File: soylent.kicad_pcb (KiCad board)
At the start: 2 copper layers, 33 x 42.2 mm, 31 parts, among them J1 DB9_Female, J2 Conn_01x04, J3 Conn_01x04, J4 Conn_02x03_Counter_Clockwise, Q1 BC847, Q2 BC847, U1 ATtiny202-SS, U2 MIC5504-3.3YM5, U3 LM2776, U4 MAX3188EEUT+T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

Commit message: Shrink required board area
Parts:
- moved J4 5.50 mm to (236.7, 30.7)
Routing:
- net Net-(J4-Pad1): track 9.78 -> 5.02 mm
- net Net-(J4-Pad3): track 13.6 -> 9.86 mm
- net Net-(J4-Pad2): track 12.9 -> 9.75 mm
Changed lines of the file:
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@@
     (thickness 1.6)
     (drawings 6)
-    (tracks 194)
+    (tracks 192)
     (zones 0)
     (modules 31)
@@
   )
   (module Pin_Headers:Pin_Header_Straight_2x03_Pitch2.54mm (layer F.Cu)
-    (at 236.6922 25.2476 90)
+    (at 236.6922 30.7476 90)
     (descr "Through hole straight pin header, 2x03, 2.54mm pitch, double rows")
     (tags "Through hole pin header THT 2x03 2.54mm double row")
@@
   (segment (start 244.0826 49.90101) (end 244.0826 49.1616) (width 0.25) (layer F.Cu) (net 6))
   (segment (start 247.04759 52.866) (end 244.0826 49.90101) (width 0.25) (layer F.Cu) (net 6))
-  (segment (start 240.407201 24.683599) (end 240.407201 26.204801) (width 0.25) (layer F.Cu) (net 7))
-  (segment (start 239.796201 24.072599) (end 240.407201 24.683599) (width 0.25) (layer F.Cu) (net 7))
-  (segment (start 245.1554 30.953) (end 245.3054 30.953) (width 0.25) (layer F.Cu) (net 7))
-  (segment (start 240.407201 26.204801) (end 245.1554 30.953) (width 0.25) (layer F.Cu) (net 7))
-  (segment (start 238.057199 24.072599) (end 239.796201 24.072599) (width 0.25) (layer F.Cu) (net 7))
-  (segment (start 236.6922 22.7076) (end 238.057199 24.072599) (width 0.25) (layer F.Cu) (net 7))
+  (segment (start 244.4554 30.953) (end 245.3054 30.953) (width 0.25) (layer F.Cu) (net 7))
+  (segment (start 237.867201 29.382601) (end 242.885001 29.382601) (width 0.25) (layer F.Cu) (net 7))
+  (segment (start 242.885001 29.382601) (end 244.4554 30.953) (width 0.25) (layer F.Cu) (net 7))
+  (segment (start 236.6922 28.2076) (end 237.867201 29.382601) (width 0.25) (layer F.Cu) (net 7))
   (segment (start 251.9553 49.9744) (end 252.2728 49.9744) (width 0.25) (layer F.Cu) (net 8))
   (segment (start 251.3878 50.5419) (end 251.9553 49.9744) (width 0.25) (layer F.Cu) (net 8))
@@
   (segment (start 235.4022 47.3732) (end 236.2708 46.5046) (width 0.25) (layer B.Cu) (net 15))
   (segment (start 233.3578 47.3732) (end 235.4022 47.3732) (width 0.25) (layer B.Cu) (net 15))
-  (segment (start 232.3234 35.195) (end 231.6734 35.195) (width 0.25) (layer F.Cu) (net 16))
-  (segment (start 233.869399 33.940003) (end 232.614402 35.195) (width 0.25) (layer F.Cu) (net 16))
-  (segment (start 232.614402 35.195) (end 232.3234 35.195) (width 0.25) (layer F.Cu) (net 16))
-  (segment (start 233.869399 30.610401) (end 233.869399 33.940003) (width 0.25) (layer F.Cu) (net 16))
-  (segment (start 239.2322 25.2476) (end 233.869399 30.610401) (width 0.25) (layer F.Cu) (net 16))
-  (segment (start 232.7734 32.701) (end 232.7734 33.401) (width 0.25) (layer F.Cu) (net 17))
-  (segment (start 233.1974 32.277) (end 232.7734 32.701) (width 0.25) (layer F.Cu) (net 17))
-  (segment (start 233.1974 30.607) (end 233.1974 32.277) (width 0.25) (layer F.Cu) (net 17))
-  (segment (start 236.6922 27.1122) (end 233.1974 30.607) (width 0.25) (layer F.Cu) (net 17))
-  (segment (start 236.6922 25.2476) (end 236.6922 27.1122) (width 0.25) (layer F.Cu) (net 17))
+  (segment (start 238.382201 31.597599) (end 239.2322 30.7476) (width 0.25) (layer F.Cu) (net 16))
+  (segment (start 235.101397 31.922601) (end 238.057199 31.922601) (width 0.25) (layer F.Cu) (net 16))
+  (segment (start 233.869399 33.154599) (end 235.101397 31.922601) (width 0.25) (layer F.Cu) (net 16))
+  (segment (start 238.057199 31.922601) (end 238.382201 31.597599) (width 0.25) (layer F.Cu) (net 16))
+  (segment (start 233.869399 33.940003) (end 233.869399 33.154599) (width 0.25) (layer F.Cu) (net 16))
+  (segment (start 232.614402 35.195) (end 233.869399 33.940003) (width 0.25) (layer F.Cu) (net 16))
+  (segment (start 231.6734 35.195) (end 232.614402 35.195) (width 0.25) (layer F.Cu) (net 16))
+  (segment (start 232.9434 33.401) (end 232.7734 33.401) (width 0.25) (layer F.Cu) (net 17))
+  (segment (start 235.5968 30.7476) (end 232.9434 33.401) (width 0.25) (layer F.Cu) (net 17))
+  (segment (start 236.6922 30.7476) (end 235.5968 30.7476) (width 0.25) (layer F.Cu) (net 17))
   (segment (start 253.2228 48.2116) (end 253.2228 47.1311) (width 0.25) (layer F.Cu) (net 18))
   (segment (start 252.2728 49.1616) (end 253.2228 48.2116) (width 0.25) (layer F.Cu) (net 18))

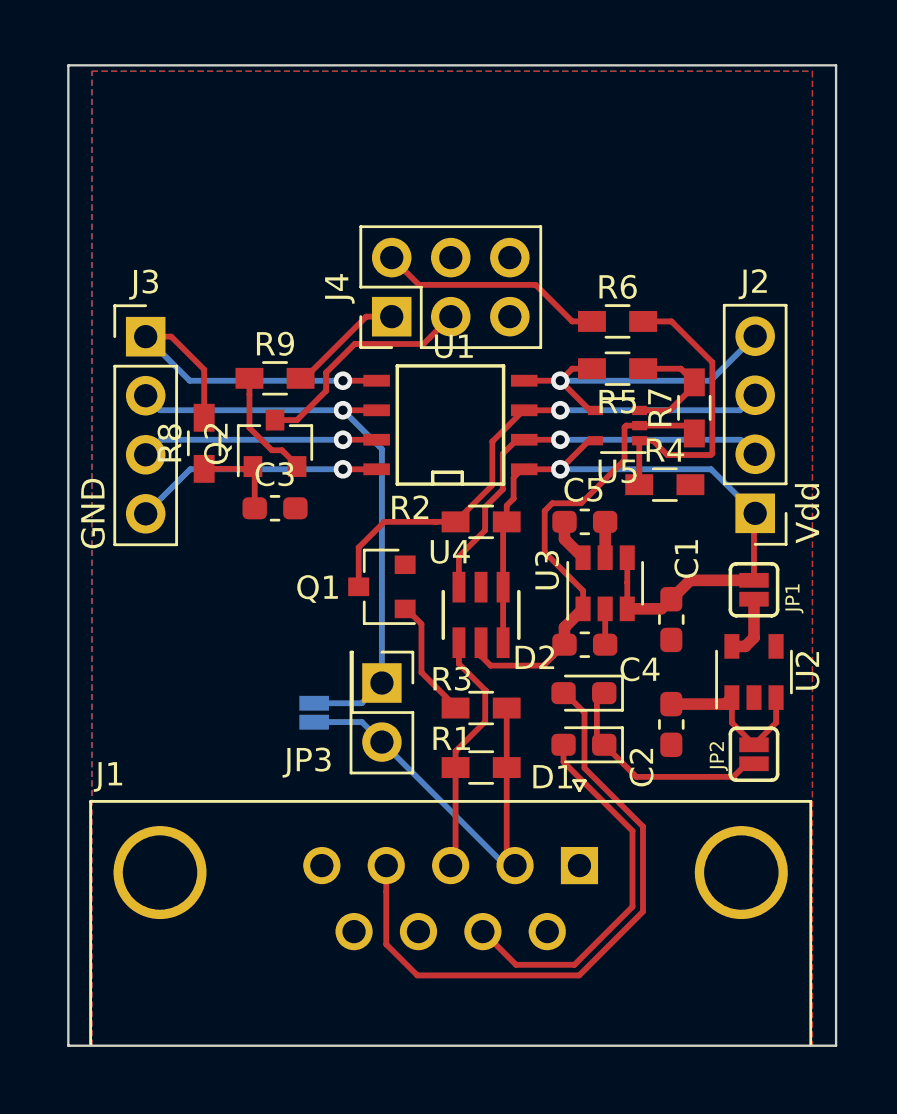
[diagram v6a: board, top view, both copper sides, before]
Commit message: Add and route trimmer pot
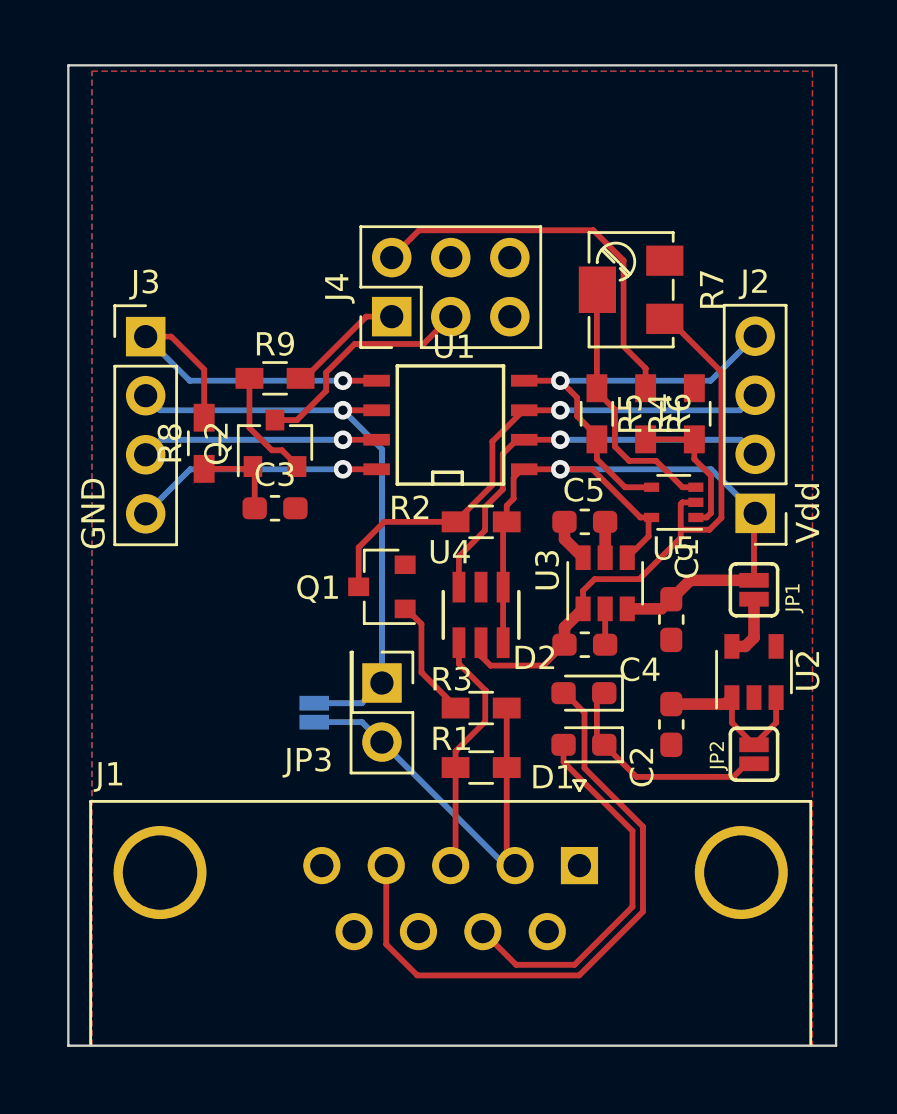
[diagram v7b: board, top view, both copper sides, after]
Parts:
- R7: value 150k -> RTRIM; footprint Resistors_SMD:R_0603_HandSoldering -> Potentiometers:Potentiometer_Trimmer_Bourns_3214W
- moved R7 5.76 mm to (247.0, 29.6), turned to 270 degrees
- moved R6 4.15 mm to (247.6, 34.9), turned to 270 degrees
- moved U5 4.09 mm to (248.8, 38.7)
- moved R4 3.30 mm to (249.7, 34.9), turned to 90 degrees
- moved R5 2.13 mm to (245.5, 34.9), turned to 270 degrees
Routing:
- net Net-(J4-Pad2): track 9.75 -> 16.9 mm
- net Net-(R4-Pad1): track 12.9 -> 6.29 mm
- net Net-(R5-Pad1): track 5.39 -> 11.3 mm
- net VEE: track 20.4 -> 26.3 mm
- net /WIN: track 14.3 -> 17.7 mm
- net VDD: track 31.7 -> 34.4 mm

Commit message: Minor prettification
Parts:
- moved U5 0.53 mm to (248.3, 38.6)
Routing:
- net VEE: track 26.3 -> 30.8 mm
- net VDD: track 34.4 -> 31.8 mm
- net /WIN: track 17.7 -> 17.0 mm
- net Net-(R4-Pad1): track 6.29 -> 5.64 mm
- net Net-(R5-Pad1): track 11.3 -> 10.7 mm
